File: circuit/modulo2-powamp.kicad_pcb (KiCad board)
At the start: 2 copper layers, 100 x 48 mm, 79 parts, among them J1 HOLE, J2 HOLE, J3 HOLE, J4 HOLE, J5 CONN_01X04, J6 CONN_01X04, SW1 reset, SW2 mute, SW3 HEAD/AD, SW4 vddsel, SW5 avdd5v, U1 LM1117-5.0, U2 TPA3220, U3 MCP16331

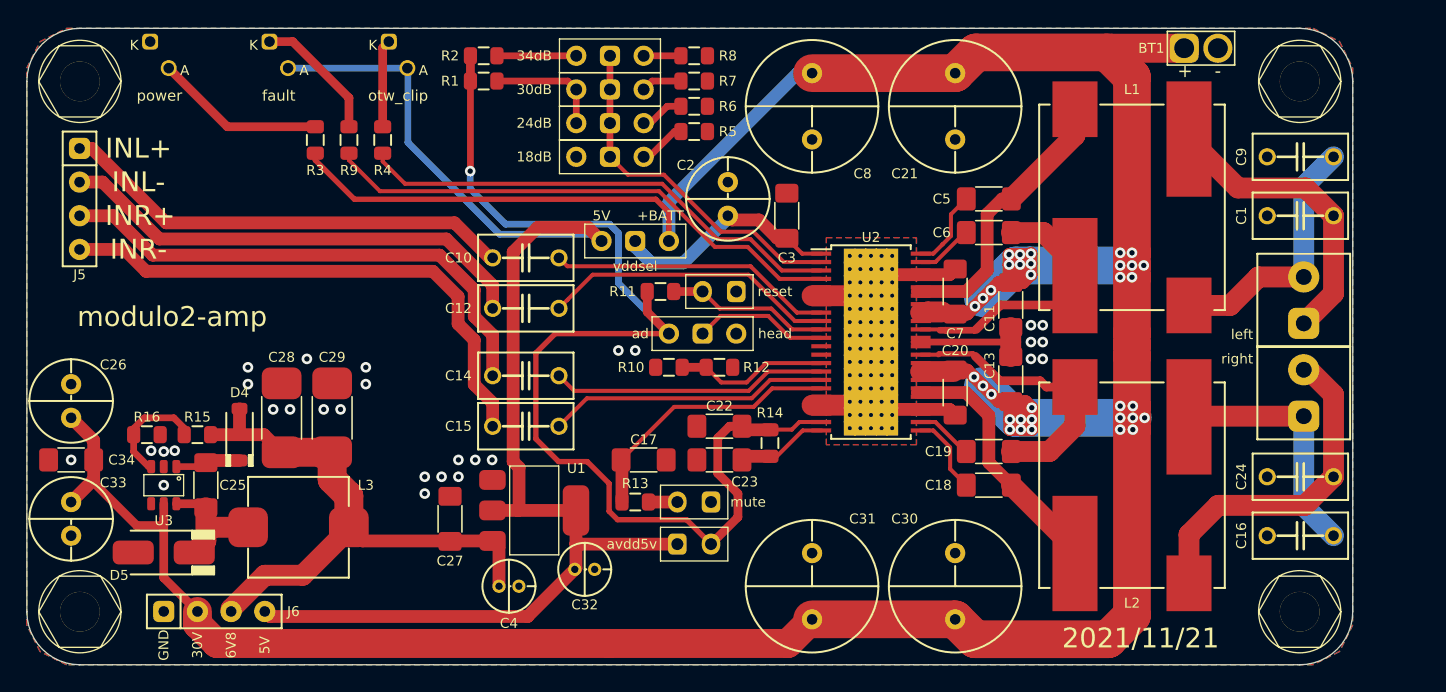
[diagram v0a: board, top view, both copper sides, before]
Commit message: Added master volume
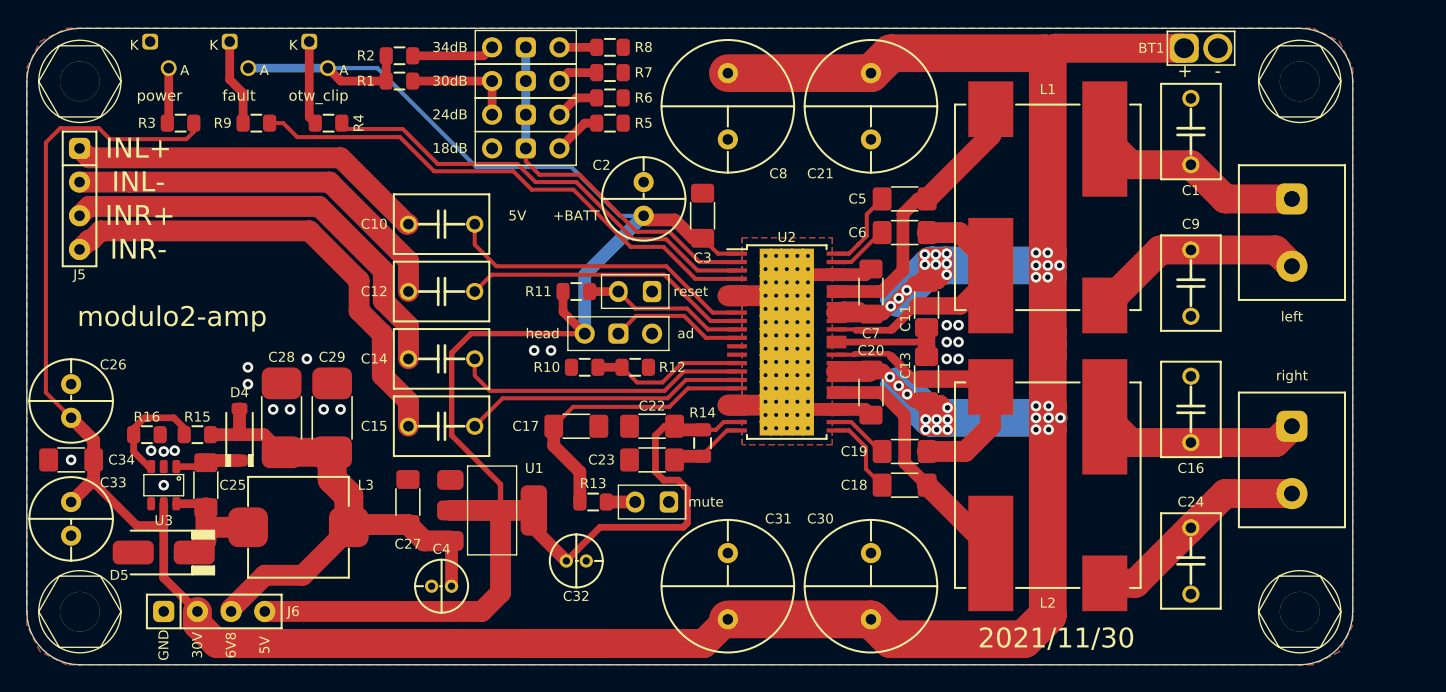
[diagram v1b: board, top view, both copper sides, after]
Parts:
- removed SW4: vddsel, myAmp:SW_SPDT_JUMPER
- removed SW5: avdd5v, myAmp:Switch_2.5mm
- C1, C10, C12, C14, C15, C16, C24, C9: footprint myAmp:C_FILM_5MM -> myAmp:C_FILM_P5mm_W4mm
- SPK1, SPK2: footprint myAmp:SPKR_3.5MM -> myAmp:SPKR_5MM_BLUE
- moved C16 12.6 mm to (137.8, 78.7), turned to 90 degrees
- moved C9 12.6 mm to (137.8, 69.2), turned to 90 degrees
- moved C1 10.4 mm to (137.8, 57.8), turned to 90 degrees
- moved C24 10.4 mm to (137.8, 90.2), turned to 90 degrees
- moved R3 10.2 mm to (61.6, 57.1), turned to 180 degrees
- moved R9 7.10 mm to (67.3, 57.1), turned to 180 degrees
- moved C10 6.84 mm to (81.3, 64.8)
- moved C12 6.48 mm to (81.3, 69.8)
- moved C14 6.48 mm to (81.3, 74.9)
- moved S1 6.38 mm to (87.6, 59.1)
- moved S2 6.38 mm to (87.6, 56.5)
- moved S3 6.38 mm to (87.6, 54.0)
- moved S4 6.38 mm to (87.6, 51.4)
- moved R6 6.38 mm to (94.0, 55.2)
- moved R5 6.38 mm to (94.0, 57.1)
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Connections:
- C2 pad 1: /VDD -> +5V
- C22 pad 1: /AVDD -> +5V
- C3 pad 2: /VDD -> +5V
- R1 pad 1: /AVDD -> +5V
- R11 pad 2: /AVDD -> +5V
- R14 pad 2: /AVDD -> +5V
- R2 pad 1: /AVDD -> +5V
- SW3 pad 1: /AVDD -> +5V
- U2 pad 1: /VDD -> +5V
- U2 pad 21: /AVDD -> +5V
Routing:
- net /AVDD: track 88.7 -> 0.00 mm, vias 1 -> 0
- net +5V: track 103.3 -> 149.3 mm
- net /VDD: track 17.7 -> 0.00 mm
- net +BATT: track 280.8 -> 271.9 mm
- net Net-(D1-Pad2): track 12.9 -> 4.19 mm
- net Net-(C24-Pad2): track 25.6 -> 16.9 mm
- net Net-(C10-Pad1): track 34.6 -> 27.2 mm
- net Net-(C12-Pad1): track 36.1 -> 29.6 mm
- net Net-(C14-Pad1): track 39.1 -> 32.6 mm
- net Net-(C1-Pad1): track 22.3 -> 16.0 mm
- net Net-(C15-Pad1): track 40.9 -> 35.7 mm
- net Net-(D3-Pad1): track 10.2 -> 6.57 mm
- net Net-(C16-Pad1): track 18.6 -> 15.4 mm
- net Net-(C9-Pad2): track 19.5 -> 16.4 mm
- net 6V8: track 44.4 -> 41.2 mm
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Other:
- board text added: "2021/11/30"
- board text removed: "2021/11/21"
- board text removed: "Power selection note: if VDD is connected to +5V (through vddsel), then AVDD must also be connected to +5V (avdd5v must be closed!) if VDD is connected to +BATT (through vddsel), then AVDD is not connected to +5V (avdd5v must be open!)"

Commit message: cleanup the the power amp a bit; still need to move the diff inputs
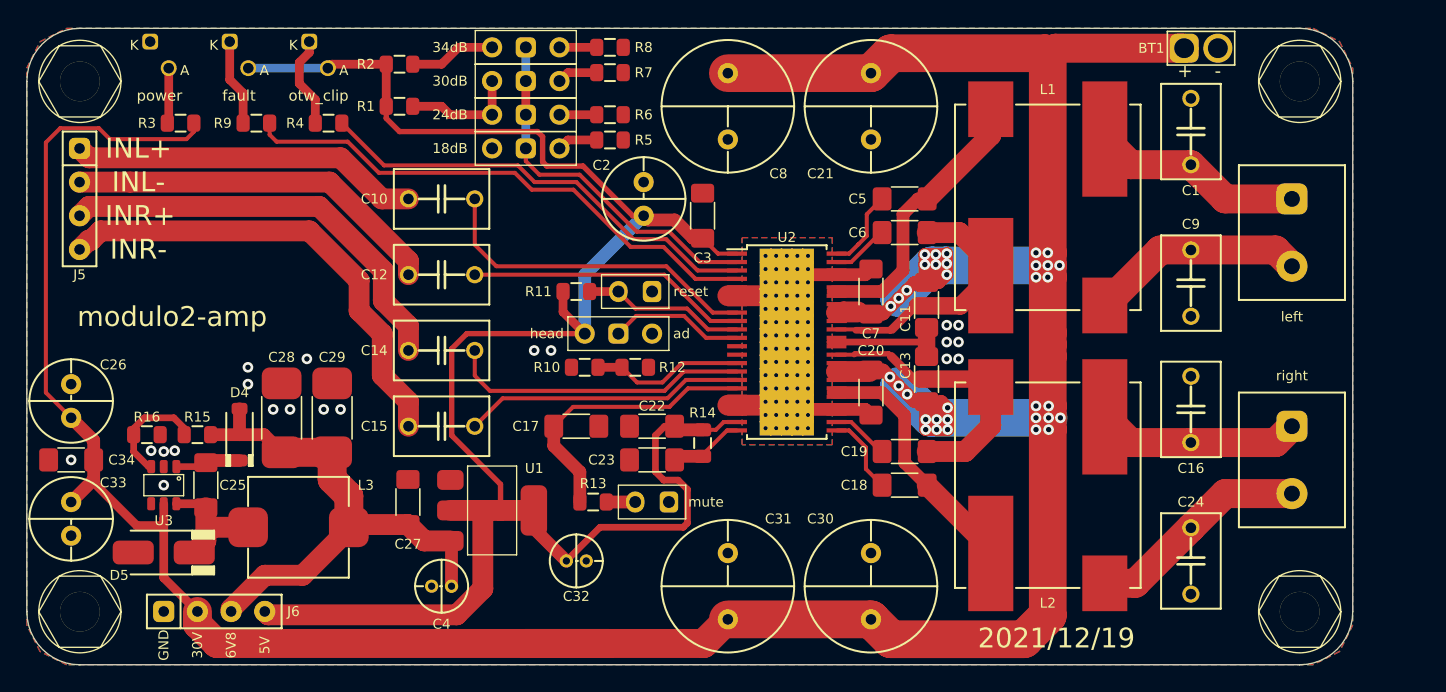
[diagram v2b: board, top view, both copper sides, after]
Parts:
- moved R1 1.91 mm to (78.1, 55.9)
- moved C10 1.90 mm to (81.3, 62.9)
- moved R5 1.27 mm to (94.0, 58.4)
- moved R6 1.27 mm to (94.0, 56.5)
- moved C12 1.27 mm to (81.3, 68.6)
- moved C14 0.64 mm to (81.3, 74.3)
- moved R2 0.63 mm to (78.1, 52.7)
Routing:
- net +5V: track 149.3 -> 145.0 mm
- net Net-(C10-Pad2): track 23.5 -> 25.4 mm
- net Net-(C12-Pad1): track 29.6 -> 28.3 mm
- net Net-(C10-Pad1): track 27.2 -> 26.4 mm
- net Net-(C14-Pad1): track 32.6 -> 32.0 mm
- net Net-(D2-Pad1): track 6.34 -> 6.96 mm
- net Net-(R6-Pad1): track 3.34 -> 2.81 mm
- net Net-(R5-Pad1): track 3.60 -> 3.07 mm
- net Net-(C12-Pad2): track 21.8 -> 21.2 mm
- net FAULT: track 40.1 -> 40.6 mm
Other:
- board text added: "2021/12/19"
- board text removed: "+BATT"
- board text removed: "2021/11/30"

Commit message: FV-1 firmware reworked for the new board; FV-1 PCB needs rework to correct errors
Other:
- net class Default removed

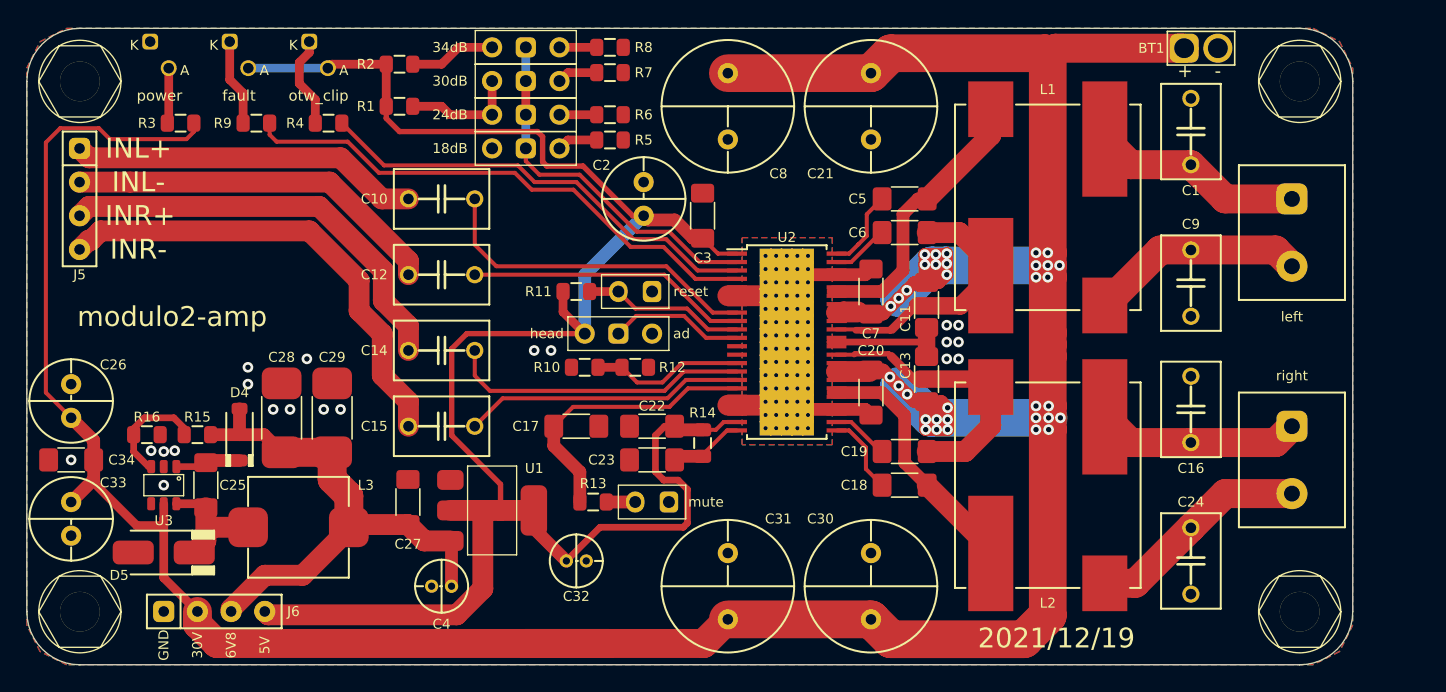
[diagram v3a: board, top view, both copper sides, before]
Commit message: added report on createBanks.py; started PCB redesign
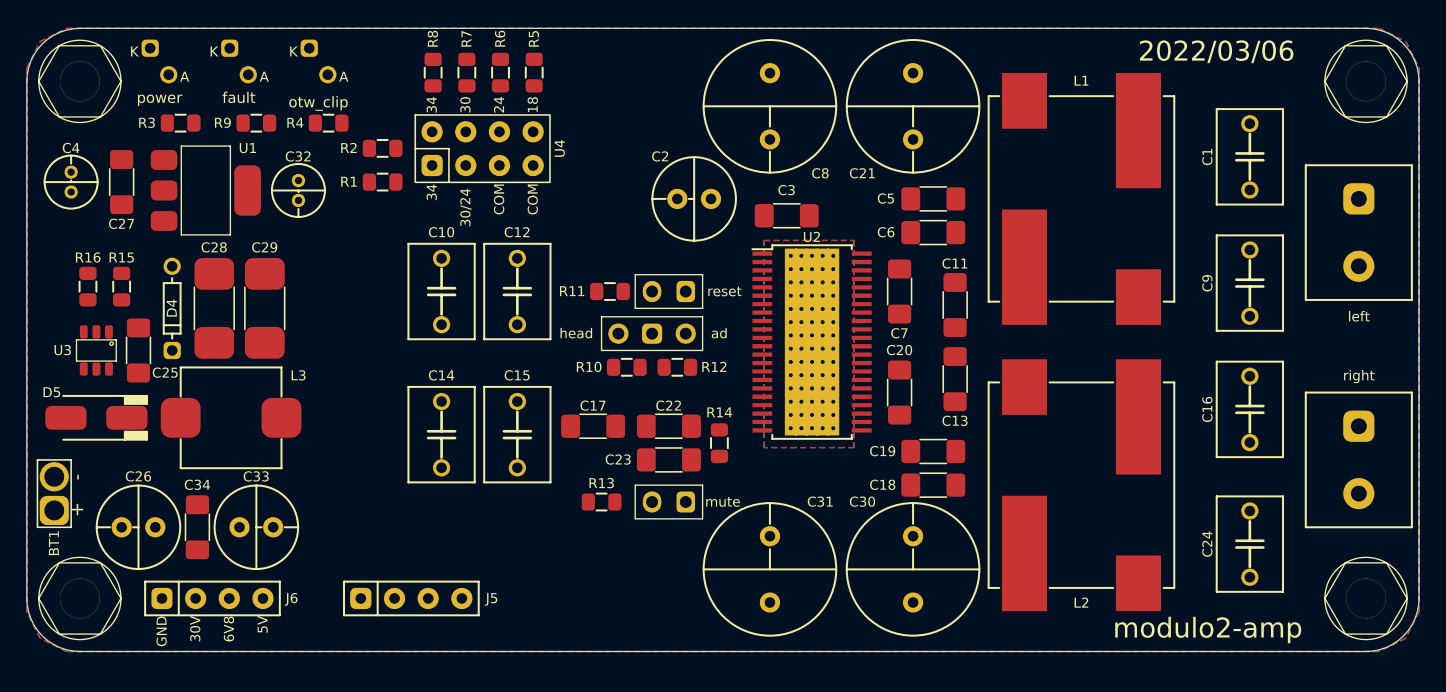
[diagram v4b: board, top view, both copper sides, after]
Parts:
- removed S1: 18dB, myAmp:JUMPER_3WAY
- removed S2: 24dB, myAmp:JUMPER_3WAY
- removed S3: 30dB, myAmp:JUMPER_3WAY
- removed S4: 34dB, myAmp:JUMPER_3WAY
- added U4: GAINSEL, myAmp:GAINSEL, F.Cu at (84.4, 59.1)
- C1, C10, C12, C14, C15, C16, C24, C9: footprint myAmp:C_FILM_P5mm_W4mm -> myAmp:C_FILM_L7.2mm_W5.0mm_P5.00mm
- D4: footprint myAmp:D_SOD-123 -> myAmp:DO35
- J6: value CONN_01X04 -> POWER; footprint myAmp:PIN_1x04 -> myAmp:POWER
- moved BT1 92.8 mm to (52.1, 85.1), turned to 90 degrees
- moved C4 41.3 mm to (53.3, 61.6), turned to 90 degrees
- moved J5 39.2 mm to (79.0, 93.0), turned to 0 degrees
- moved C32 34.9 mm to (70.5, 62.2), turned to -90 degrees
- moved U1 32.4 mm to (63.5, 62.2)
- moved C27 32.4 mm to (57.1, 61.6)
- moved C33 14.0 mm to (67.3, 87.6), turned to 0 degrees
- moved R8 13.5 mm to (80.6, 53.3), turned to 90 degrees
- moved R15 12.5 mm to (57.1, 69.5), turned to -90 degrees
- moved R16 12.0 mm to (54.6, 69.5), turned to 90 degrees
- moved D5 11.4 mm to (55.2, 79.4)
- moved U3 11.4 mm to (55.2, 74.3)
- moved C25 11.4 mm to (58.4, 74.3)
- moved R7 10.8 mm to (83.2, 53.3), turned to 90 degrees
- moved C34 10.8 mm to (62.9, 87.6), turned to 90 degrees
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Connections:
- J1 pad 1: (no net) -> unconnected-(J1-Pad1)
- J2 pad 1: (no net) -> unconnected-(J2-Pad1)
- J3 pad 1: (no net) -> unconnected-(J3-Pad1)
- J4 pad 1: (no net) -> unconnected-(J4-Pad1)
- U2 pad 12: (no net) -> unconnected-(U2-Pad12)
- U2 pad 13: (no net) -> unconnected-(U2-Pad13)
- U3 pad 4: (no net) -> unconnected-(U3-Pad4)
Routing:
- net +BATT: track 271.9 -> 0.00 mm, vias 34 -> 0
- net +5V: track 145.0 -> 0.00 mm
- net GND: track 99.0 -> 0.00 mm, vias 20 -> 0
- net 6V8: track 41.2 -> 0.00 mm
- net FAULT: track 40.6 -> 0.00 mm
- net Net-(C15-Pad1): track 35.7 -> 0.00 mm
- net OTW_CLIP: track 34.4 -> 0.00 mm
- net Net-(C14-Pad1): track 32.0 -> 0.00 mm
- net Net-(C12-Pad1): track 28.3 -> 0.00 mm
- net Net-(U2-Pad2): track 27.0 -> 0.00 mm
- net Net-(C10-Pad1): track 26.4 -> 0.00 mm
- net Net-(C10-Pad2): track 25.4 -> 0.00 mm
- net Net-(C14-Pad2): track 22.1 -> 0.00 mm
- net /CMUTE: track 21.5 -> 0.00 mm
- net /OUT1_P: track 21.2 -> 0.00 mm
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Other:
- board size 100 x 48 mm -> 105 x 47 mm
- board text added: "2022/03/06"
- board text removed: "2021/12/19"
- board text removed: "30V"
- board text removed: "5V"
- board text removed: "6V8"
- board text removed: "GND"
- board text removed: "INL+"
- board text removed: "INL-"
- board text removed: "INR+"
- board text removed: "INR-"

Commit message: routing powamp
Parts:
- moved R15 0.69 mm to (56.5, 69.2)
- moved R16 0.69 mm to (54.0, 69.2)
- moved C34 0.63 mm to (62.9, 87.0)
- moved L2 0.25 mm to (129.5, 84.2)
- moved U4 0.08 mm to (84.5, 59.1)
- turned C2 to 90 degrees
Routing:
- net +BATT: track 0.00 -> 215.1 mm
- net +5V: track 0.00 -> 68.3 mm
- net 6V8: track 0.00 -> 50.6 mm
- net Net-(C24-Pad2): track 0.00 -> 19.4 mm
- net Net-(C1-Pad1): track 0.00 -> 18.8 mm
- net Net-(C9-Pad2): track 0.00 -> 18.6 mm
- net Net-(C16-Pad1): track 0.00 -> 17.9 mm
- net Net-(C25-Pad1): track 0.00 -> 10.2 mm
- net /OUT1_P: track 0.00 -> 9.54 mm
- net Net-(R1-Pad2): track 0.00 -> 7.13 mm
- net /OUT1_M: track 0.00 -> 6.26 mm
- net Net-(D3-Pad1): track 0.00 -> 6.07 mm
- net Net-(D2-Pad1): track 0.00 -> 5.84 mm
- net Net-(C25-Pad2): track 0.00 -> 5.59 mm
- net Net-(R15-Pad2): track 0.00 -> 5.35 mm
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
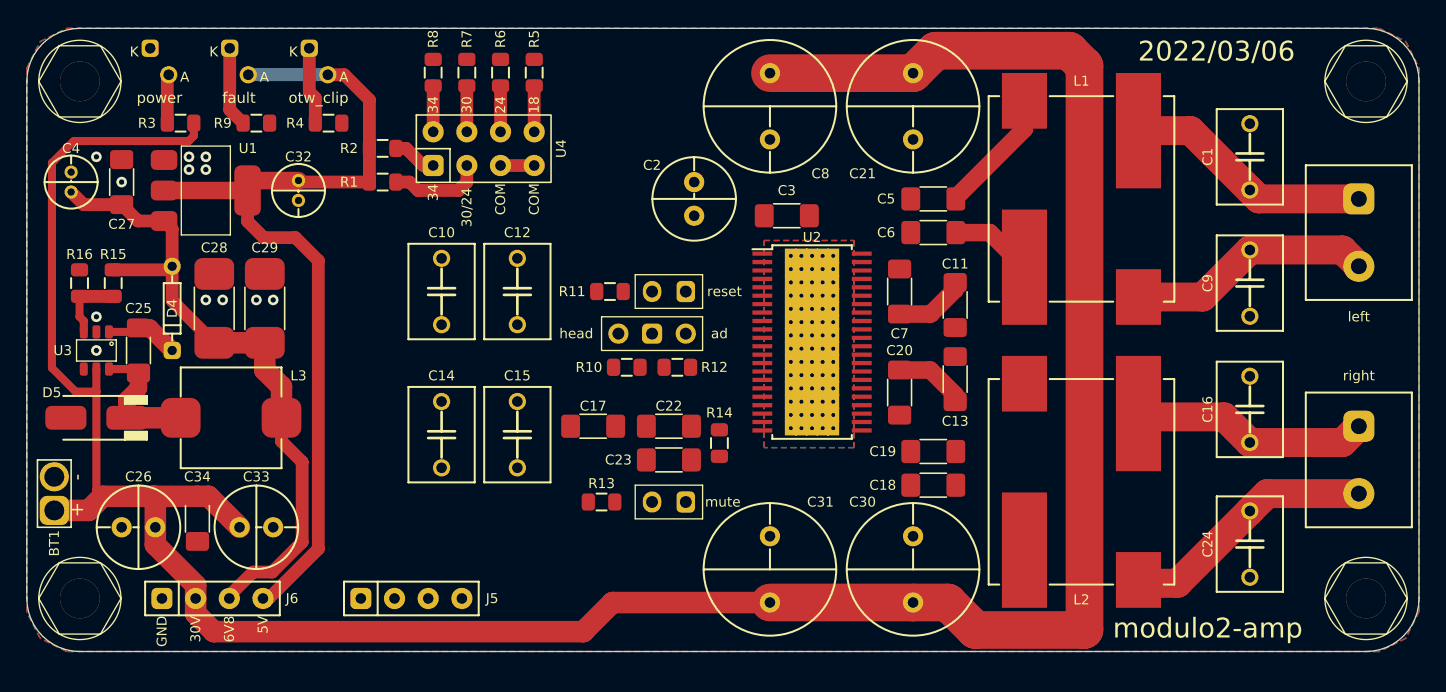
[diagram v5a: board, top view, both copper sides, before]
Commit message: routed pa27; routing fv-1
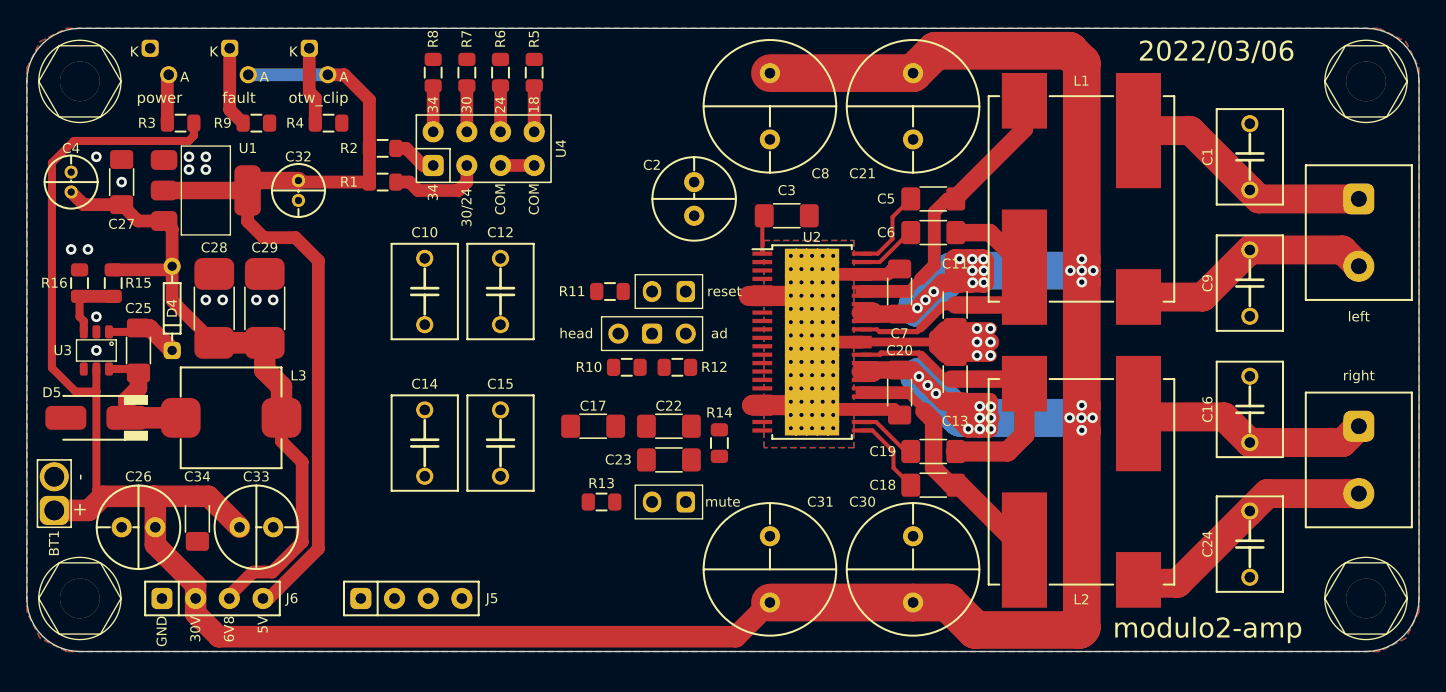
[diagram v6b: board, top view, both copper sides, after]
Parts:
- moved C15 1.42 mm to (85.7, 81.3)
- moved C14 1.42 mm to (80.0, 81.3)
- moved C12 1.27 mm to (85.7, 69.8)
- moved C10 1.27 mm to (80.0, 69.8)
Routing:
- net +BATT: track 215.1 -> 273.7 mm, vias 0 -> 30
- net GND: track 0.00 -> 47.0 mm, vias 12 -> 20
- net /OUT2_P: track 0.00 -> 22.8 mm
- net /OUT2_M: track 0.00 -> 20.0 mm
- net /OUT1_P: track 9.54 -> 22.5 mm
- net /OUT1_M: track 6.26 -> 18.4 mm
- net Net-(C5-Pad1): track 0.00 -> 6.36 mm
- net Net-(C18-Pad2): track 0.00 -> 6.13 mm
- net Net-(C19-Pad2): track 0.00 -> 4.61 mm
- net Net-(C6-Pad1): track 0.00 -> 4.61 mm
- net +5V: track 68.3 -> 71.2 mm
